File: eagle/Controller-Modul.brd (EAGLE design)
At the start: 100 x 61 mm, 53 parts, among them IC2 7805TV, Q6 BC550C, Q7 BC560, U1 ATTINY85-20S, X1 MKDSN1,5/2-5,08, X2 MKDSN1,5/2-5,08, X4 MKDSN1,5/2-5,08

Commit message: pcb design
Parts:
- removed C1, C5, C6: 100nF, rcl:C0805
- removed C2: 100µ, resistor:E2,5-7
- removed C3: (no value), rcl:C0603K
- removed C4: 1000µ, rcl:E3,5-8
- removed D1: 18V, diode:SOD80C
- removed D2: (no value), diode:SOT23
- removed D3: 1N4004, diode:DO41-10
- removed IC1: (no value), v-reg:317TS
- removed IC2: 7805TV, linear:TO220V
- removed LED1: (no value), led:LED3MM
- removed Q2, Q3, Q4, Q5: (no value), transistor-power:TO220BV
- removed Q6: BC550C, transistor-npn:TO92-EBC
- removed Q7: BC560, transistor-pnp:TO92-EBC
- removed R15: 1k, resistor:R1206
- removed R16, R18, R19: 33k, resistor:R1206
- removed R17: 10k, resistor:R1206
- removed R20: 100k, rcl:R1206
- removed R21: (no value), pot:PT-10
- removed R5, R6, R7: (no value), resistor:0207/10
- removed TR1, TR2: (no value), trafo:EI38-1
- removed U$1: GLEICHRICHTER, Gleichrichter:KBPC1
- removed U1: ATTINY85-20S, _hhn_attiny25_45_85:SOIC8_EIAJ_208MIL
- removed X1, X2, X4: MKDSN1,5/2-5,08, con-phoenix-508:MKDSN1,5/2-5,08
- added 1: SUMMER4, 0liver:PIEZO-INDIKATOR-KPMG
- added C10, C11: 22pF, resistor:C0603K
- added C12: 100 nF, resistor:C0603
- added C9: 1n, rcl:C0603K
- added D4, D5, D6: (no value), diode:SOT23
- added IC3: ATMEGA328P, avr-6:DIL28-3
- added JP10, JP4, JP6: (no value), pinhead:1X02
- added JP5: (no value), pinhead:1X04
- added JP7: (no value), pinhead:1X16
- added JP8: (no value), pinhead:2X03
- added JP9: (no value), pinhead:1X03
- C7: value 100nF -> 1n; device rcl:C0805 -> rcl:C0603K
- C8: value 100µ -> 1n; device rcl:E3,5-8 -> rcl:C0603K
- JP2: device pinhead:2X03 -> pinhead:1X02
- Q1: value (none) -> BC550C; device transistor-power:TO220BV -> transistor-npn:TO92-EBC
- R10, R8: value (none) -> 300; device resistor:0207/10 -> resistor:R1206
- R11: value (none) -> 10k; device resistor:0207/10 -> pot:PT-10
- R12: value 100k -> 2k7; device rcl:R1206 -> resistor:R1206
- R13: value 10k -> 300
- R14: value 33k -> 2k7
- R2: value (none) -> 10k; device resistor:0207/10 -> resistor:R1206
- R3: value (none) -> 33k; device resistor:0207/10 -> resistor:R1206
- R4: value (none) -> 220; device resistor:0207/10 -> resistor:R1206
- R9: value (none) -> 2k7; device resistor:0207/10 -> resistor:R1206
- U$2: value GLEICHRICHTER -> ABRACON_ABM3_CRYSTALABM03_HC49; device Gleichrichter:KBPC1 -> Ava:ABM03_HC49
- moved JP3 382.6 mm to (34.3, 54.6), turned to 270 degrees
- moved JP1 369.8 mm to (48.3, 54.6), turned to 90 degrees
- moved R14 165.4 mm to (27.9, 48.9), flipped to the bottom, turned to 270 degrees
- moved R13 155.4 mm to (27.9, 42.5), flipped to the bottom, turned to 270 degrees
- moved R10 133.1 mm to (19.7, 42.5), flipped to the bottom, turned to 270 degrees
- moved R9 131.5 mm to (11.4, 48.9), flipped to the bottom, turned to 270 degrees
- moved R8 120.7 mm to (11.4, 42.5), flipped to the bottom, turned to 270 degrees
- moved R3 119.8 mm to (48.3, 45.7), flipped to the bottom, turned to 90 degrees
- moved R2 113.9 mm to (45.1, 45.7), flipped to the bottom, turned to 90 degrees
- moved R11 110.6 mm to (6.35, 18.4)
- moved R4 97.7 mm to (45.1, 12.7), flipped to the bottom
- moved Q1 95.2 mm to (53.3, 45.1), turned to 90 degrees
- moved C8 83.7 mm to (15.9, 50.2), flipped to the bottom, turned to 180 degrees
- moved C7 79.7 mm to (7.62, 49.5), flipped to the bottom, turned to 180 degrees
- moved R12 67.4 mm to (19.7, 48.9), flipped to the bottom, turned to 270 degrees
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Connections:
- removed net +5V: C1.1, C6.1, IC2.3, JP2.2, R12.2, U1.8
- removed net N$1: Q7.B, R13.2, R14.2
- removed net N$15: R15.1
- removed net N$16: Q1.D, Q2.D, Q3.D, Q4.D, Q5.D, R19.1
- removed net N$17: C4.+, C5.1, IC2.1, U$1.+
- removed net N$19: TR1.1, X4.1
- removed net N$2: Q5.G, R11.1, R6.1
- removed net N$20: TR1.5, X4.2
- removed net N$21: TR1.7, U$1.AC2
- removed net N$22: TR1.9, U$1.AC1
- removed net N$23: R17.2, U1.2
- removed net N$25: U$2.AC2, X1.1
- removed net N$29: JP1.2, R21.A
- removed net N$3: Q6.B, R16.2, R17.1
- removed net N$30: IC1.1, JP1.1, R20.1
- removed net N$5: Q6.C, R13.1
- removed net N$7: Q3.G, R4.1, R9.1
- removed net N$8: C2.+, D1.C, Q7.E, R14.1, R15.2
- new net C1V: C7.2, D4.1, JP1.1, JP5.3, R8.1, R9.2
- new net C2V: C8.2, D5.1, JP5.1, R10.1, R12.2
- new net DATA0: IC3.4, JP7.11
- new net DATA1: IC3.5, JP7.12
- new net DATA2: IC3.6, JP7.13
- new net DATA3: IC3.11, JP7.14
- new net LED: IC3.14, R4.1
- new net N$26: IC3.15, R1.2
- new net N$31: IC3.13, JP9.2
- new net N$32: JP7.3, R11.S
- new net N$34: IC3.12, JP9.1
- new net N$47: JP7.15, R4.2
- new net RES: IC3.1, JP8.5
- new net RS: IC3.2, JP7.4
- new net RW: IC3.3, JP7.6
- new net SENV: C9.2, D6.1, JP5.4, R13.1, R14.2
- new net VCC: C12.1, IC3.20, IC3.21, IC3.7, JP10.2, JP7.2, JP8.2, Q1.C, R11.A
- net GND: now also 1.P$2, C10.2, C11.2, C12.2, IC3.22, IC3.8, JP1.2, JP10.1, JP2.1, JP3.1, JP5.2, JP6.2, JP7.1, JP7.16, JP7.5, JP8.6, JP9.3, R11.E, R12.1, R14.1, R3.2, R9.1; no longer C1.2, C2.-, C3.2, C4.-, C5.2, C6.2, C7.2, C8.-, D1.A, D2.1, IC2.2, JP2.6, JP3.2, LED1.K, Q6.E, R16.1, R18.1, R21.E, R21.S, U$1.-, U$2.-, U1.4, X2.1
- net MISO: now also IC3.18, JP8.1; no longer JP2.1, U1.6
- net MOSI: now also IC3.17, JP8.4; no longer JP2.4, U1.5
- net N$10: now also IC3.23, JP2.2; no longer JP2.5, R12.1, U1.1
- net N$11: now also JP4.1, Q1.E; no longer Q1.S, Q2.S, Q3.S, Q4.S, Q5.S, R2.2, R3.2, R4.2, R5.2, R6.2
- net N$12: now also IC3.24, JP3.2; no longer R1.2, U1.3
- net N$13: now also 1.P$1, JP4.2; no longer Q1.G, R2.1, R7.1
- net N$14: now also C7.1, D4.3, IC3.27, R8.2; no longer C3.1, D2.3, R18.2, R19.2
- net N$18: now also C9.1, D6.3, IC3.25, R13.2; no longer Q7.C, R10.2, R11.2, R7.2, R8.2, R9.2
- net N$24: now also C8.1, D5.3, IC3.26, R10.2; no longer U$2.AC1, X1.2
- net N$27: now also C11.1, IC3.10, U$2.2; no longer C7.1, C8.+, D3.C, IC1.3, U$2.+
- net N$28: now also C10.1, IC3.9, U$2.1; no longer D3.A, IC1.2, JP3.1, R20.2, X2.2
- net N$4: now also Q1.B, R2.2; no longer Q4.G, R10.1, R5.1
- net N$6: now also JP6.1; no longer LED1.A
- net N$9: now also IC3.16, R2.1; no longer Q2.G, R8.1
- net SCK: now also IC3.19, JP8.3; no longer JP2.3, U1.7
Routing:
- net GND: track 0.00 -> 166.4 mm
- net C1V: track 0.00 -> 66.9 mm
- net VCC: track 0.00 -> 46.4 mm
- net DATA3: track 0.00 -> 42.7 mm
- net SENV: track 0.00 -> 37.6 mm
- net N$6: track 0.00 -> 36.2 mm
- net N$10: track 0.00 -> 28.8 mm
- net DATA2: track 0.00 -> 26.8 mm
- net DATA1: track 0.00 -> 26.4 mm
- net DATA0: track 0.00 -> 25.7 mm
- net N$12: track 0.00 -> 25.3 mm
- net N$18: track 0.00 -> 23.3 mm
- net N$14: track 0.00 -> 22.5 mm
- net N$24: track 0.00 -> 21.7 mm
- net MISO: track 0.00 -> 20.9 mm
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- added copper zone on layer 16, net GND
- added copper zone on layer 16, net N$16
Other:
- board size 100 x 61 mm -> 100 x 60 mm

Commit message: Lots of schema and board changes
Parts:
- added JP11: (no value), pinhead:1X02
- added R5: 150, rcl:R1206
- moved JP5 36.9 mm to (58.1, 45.1)
- moved JP6 29.1 mm to (63.5, 27.3), turned to 0 degrees
- moved JP10 21.0 mm to (21.0, 43.8), turned to 90 degrees
- moved 1 13.5 mm to (63.5, 35.6)
- moved R2 13.4 mm to (46.4, 32.4)
- moved R3 13.4 mm to (49.5, 32.4)
- moved JP9 13.0 mm to (59.1, 18.4)
- moved Q1 12.7 mm to (54.0, 32.4)
- moved JP4 12.6 mm to (48.8, 43.8)
- moved JP1 12.5 mm to (41.9, 43.8)
- moved R12 12.5 mm to (16.5, 36.8)
- moved R14 12.5 mm to (24.8, 36.8)
- moved R9 12.5 mm to (8.26, 36.8)
- moved R10 12.5 mm to (16.5, 30.5)
- moved R13 12.5 mm to (24.8, 30.5)
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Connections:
- new net N$1: JP11.1, R5.1
- new net N$2: IC3.28, R5.2
- net GND: now also JP11.2
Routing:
- net GND: track 166.4 -> 287.2 mm, vias 0 -> 2
- net VCC: track 46.4 -> 158.8 mm, vias 0 -> 1
- net RES: track 3.76 -> 68.8 mm, vias 0 -> 2
- net C2V: track 11.6 -> 62.6 mm, vias 0 -> 1
- net N$6: track 36.2 -> 7.89 mm
- net SENV: track 37.6 -> 58.5 mm, vias 0 -> 1
- net N$34: track 0.00 -> 19.0 mm
- net C1V: track 66.9 -> 82.8 mm
- net N$31: track 0.00 -> 15.5 mm
- net DATA3: track 42.7 -> 31.4 mm
- net N$10: track 28.8 -> 21.7 mm
- net N$13: track 11.0 -> 16.8 mm
- net N$11: track 11.7 -> 17.4 mm
- net N$12: track 25.3 -> 20.0 mm
- net N$27: track 13.6 -> 8.81 mm
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- added copper zone on layer 1, net GND
- added copper zone on layer 1, net N$3
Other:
- board size 100 x 60 mm -> 72 x 49 mm

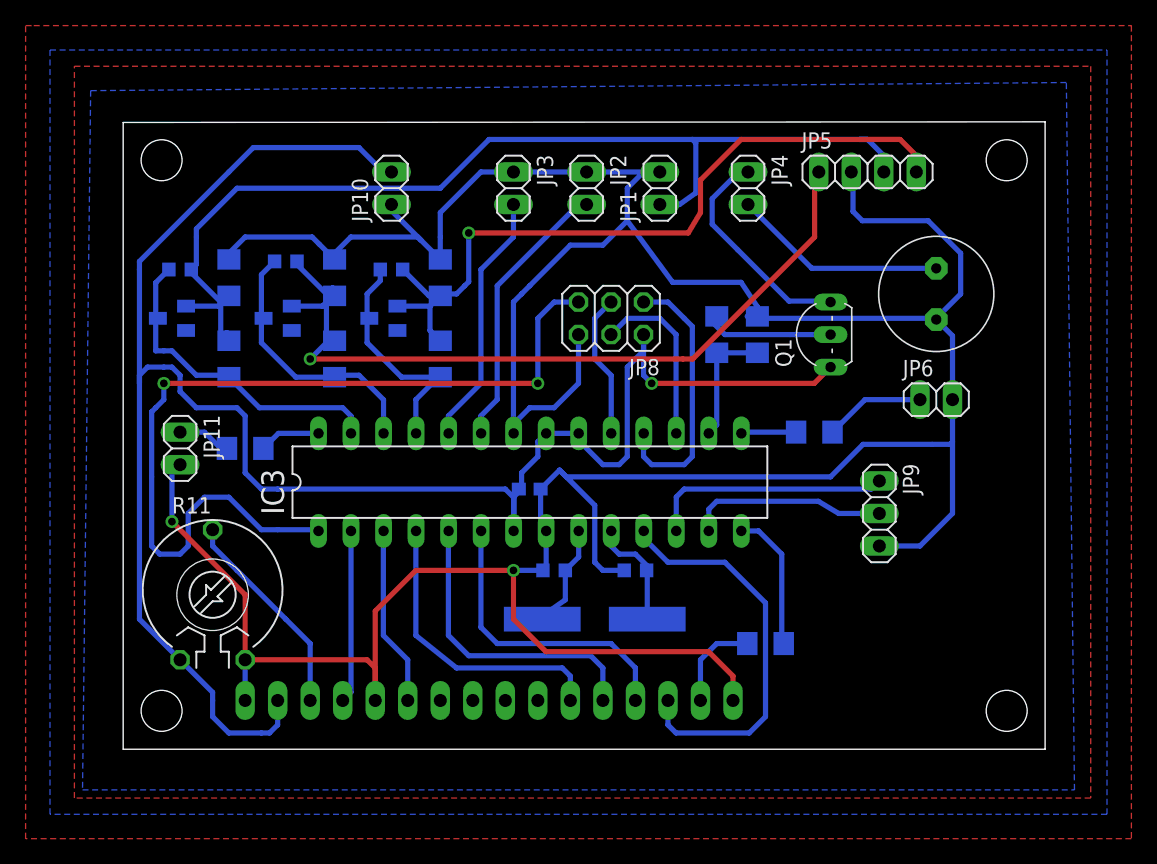
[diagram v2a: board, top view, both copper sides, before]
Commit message: Adjusted drill positions, little size corrections, new pin header
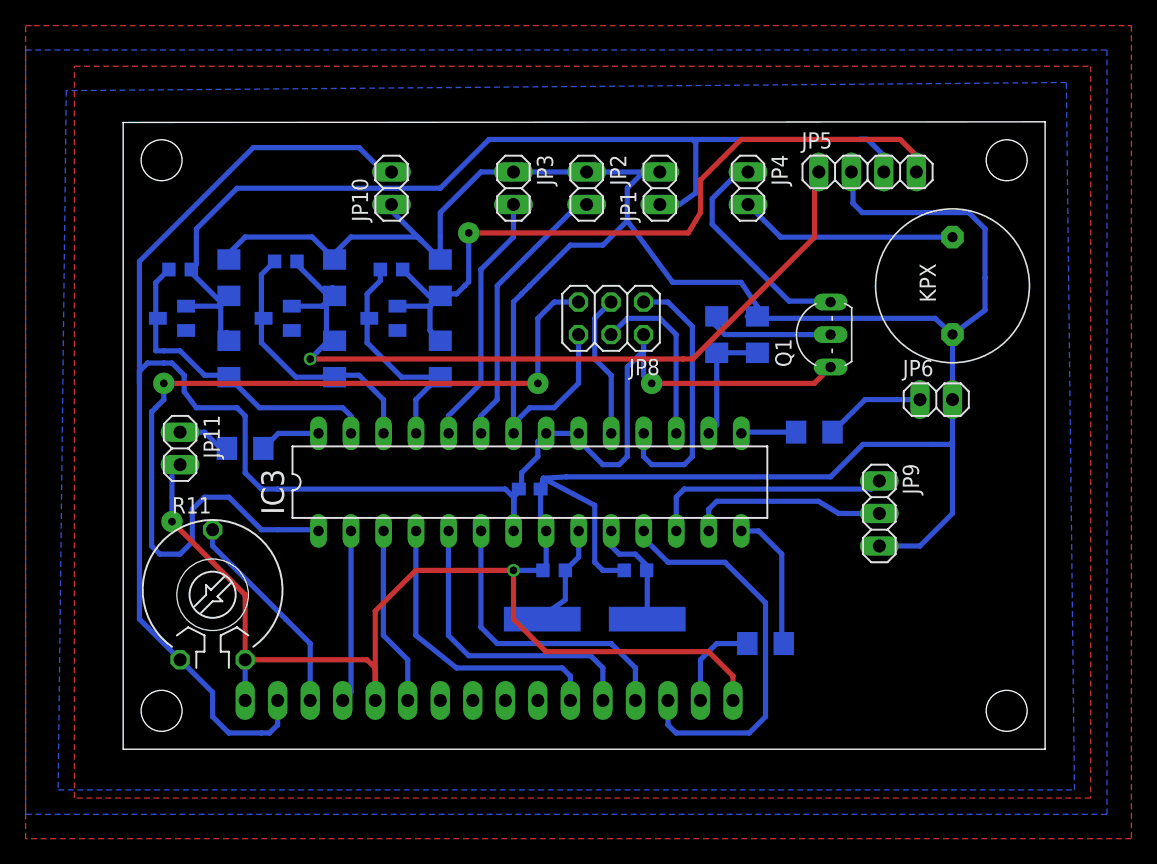
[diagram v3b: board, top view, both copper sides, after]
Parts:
- moved 1 1.42 mm to (64.8, 36.2)
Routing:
- net GND: track 287.2 -> 292.0 mm
- net VCC: track 158.8 -> 159.4 mm

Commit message: Var. Changes. Layout and new diode for 7818
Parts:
- removed C8, C9: 1n, rcl:C0603K
- removed D5, D6: (no value), diode:SOT23
- removed R10: 300, resistor:R1206
- removed R12, R14: 2k7, resistor:R1206
- added C1, C2: 1n, rcl:C0603K
- added D1, D2: (no value), diode:SOT23
- added R16, R7: 3k9, resistor:R1206
- added R6: 560, resistor:R1206
- JP9: device pinhead:1X03 -> pinhead:1X04
- R15, R8: value 300 -> 560
- R2: value 10k -> 1k
- R9: value 2k7 -> 3k9
- moved 1 30.3 mm to (59.7, 6.35)
- moved R4 1.90 mm to (50.2, 10.2)
- moved R9 1.27 mm to (9.53, 36.8)
- moved R11 0.63 mm to (7.62, 12.1)
- turned R15 to 180 degrees
- renumbered R13 to R15
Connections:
- removed net N$14: C7.1, D4.3, IC3.27, R8.2
- removed net N$24: C8.1, D5.3, IC3.26, R10.2
- new net N$5: C7.2, D4.1, IC3.27, R8.1, R9.2
- new net N$7: C1.2, D1.1, IC3.26, R6.1, R7.2
- net C1V: now also R9.1; no longer C7.2, D4.1, R8.1, R9.2
- net C2V: now also R7.1; no longer C8.2, D5.1, R10.1, R12.2
- net GND: now also C1.1, C2.1, C7.1, D1.3, D2.3, D4.3, JP9.4, R15.2, R6.2, R8.2; no longer JP9.3, R12.1, R14.1, R9.1
- net MISO: now also JP9.1
- net N$18: now also C2.2, D2.1, R15.1, R16.2; no longer C9.1, D6.3, R15.2
- net N$31: now also JP9.3; no longer JP9.2
- net N$34: now also JP9.2; no longer JP9.1
- net SENV: now also R16.1; no longer C9.2, D6.1, R14.2, R15.1
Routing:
- net GND: track 292.0 -> 419.4 mm, vias 2 -> 3
- net N$13: track 17.0 -> 49.6 mm
- net N$5: track 0.00 -> 27.0 mm
- net N$14: track 25.7 -> 0.00 mm
- net N$24: track 21.2 -> 0.00 mm
- net C1V: track 82.8 -> 64.5 mm
- net N$7: track 0.00 -> 18.2 mm
- net MISO: track 20.9 -> 35.8 mm
- net C2V: track 62.6 -> 56.0 mm, vias 1 -> 2
- net N$18: track 19.4 -> 24.5 mm
- net SENV: track 58.5 -> 54.8 mm, vias 1 -> 2
- net N$47: track 7.36 -> 9.26 mm
- net LED: track 11.0 -> 9.05 mm
- net N$31: track 15.5 -> 16.2 mm

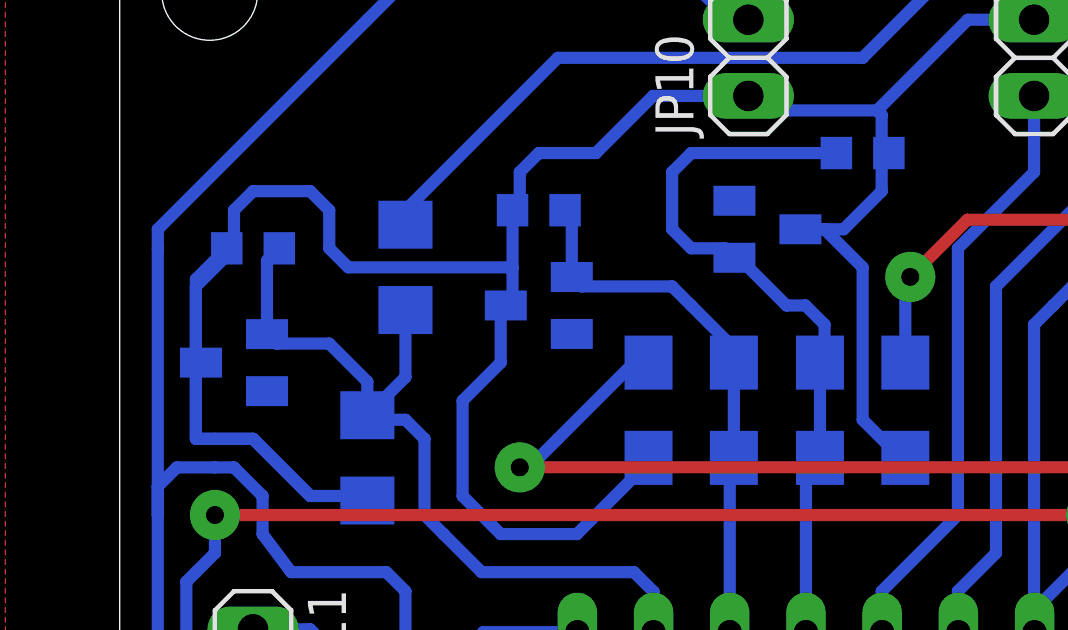
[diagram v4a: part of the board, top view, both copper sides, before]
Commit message: Corrected wrong direction of zener diodes
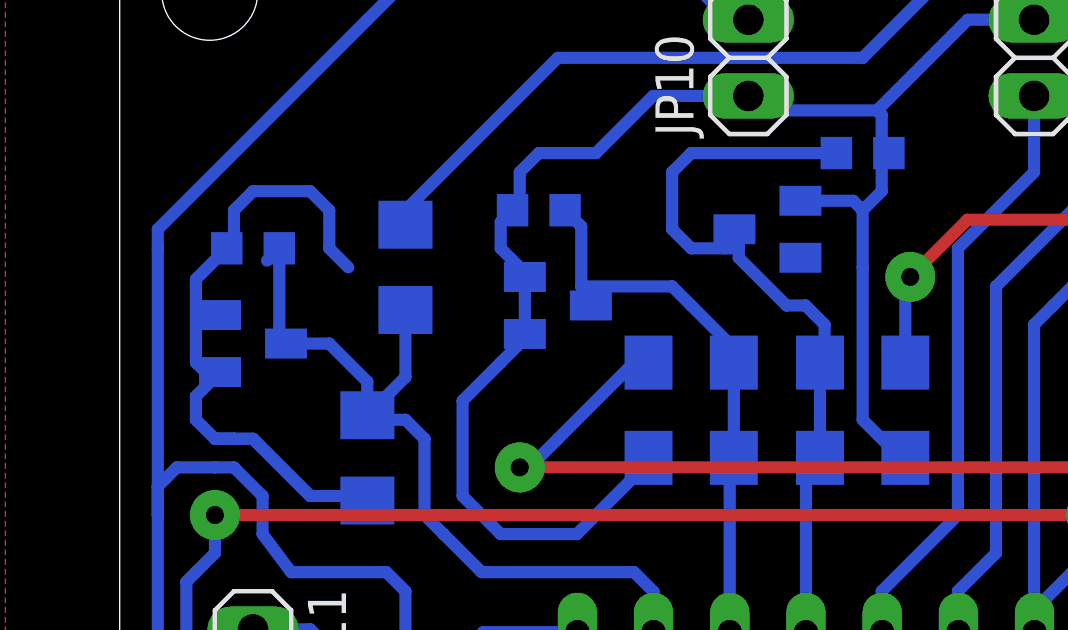
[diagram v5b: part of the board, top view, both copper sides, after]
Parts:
- moved D4 0.90 mm to (4.45, 34.3), turned to 90 degrees
- moved D1 0.63 mm to (14.6, 35.6), turned to 90 degrees
- turned D2 to 270 degrees
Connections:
- net GND: now also D1.1, D2.1, D4.1; no longer D1.3, D2.3, D4.3
- net N$18: now also D2.3; no longer D2.1
- net N$5: now also D4.3; no longer D4.1
- net N$7: now also D1.3; no longer D1.1
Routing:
- net GND: track 419.4 -> 407.2 mm
- net N$7: track 18.2 -> 19.3 mm
- net N$18: track 24.5 -> 25.4 mm
- net N$5: track 27.0 -> 27.7 mm
